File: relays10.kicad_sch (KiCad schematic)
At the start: 40 parts, among them K21 Fujitsu_FTR-LYAA005x, K22 Fujitsu_FTR-LYAA005x, K23 Fujitsu_FTR-LYAA005x, K24 Fujitsu_FTR-LYAA005x, K25 Fujitsu_FTR-LYAA005x, K26 Fujitsu_FTR-LYAA005x, K27 Fujitsu_FTR-LYAA005x, K28 Fujitsu_FTR-LYAA005x, K29 Fujitsu_FTR-LYAA005x, K30 Fujitsu_FTR-LYAA005x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

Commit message: moved to 3v3
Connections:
- net Tr1 renamed Sqr1
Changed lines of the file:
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@@
 		)
 	)
-	(global_label "Tr1"
+	(global_label "Sqr1"
 		(shape input)
 		(at 59.69 74.93 270)
@@
 		)
 		(property "Intersheetrefs" "${INTERSHEET_REFS}"
-			(at 59.69 80.8785 90)
-			(effects
-				(font
-					(size 1.27 1.27)
-				)
-				(justify right)
-				(hide yes)
-			)
-		)
-	)
-	(global_label "Tr1"
+			(at 59.69 82.2694 90)
+			(effects
+				(font
+					(size 1.27 1.27)
+				)
+				(justify right)
+				(hide yes)
+			)
+		)
+	)
+	(global_label "Sqr1"
+		(shape input)
+		(at 149.86 74.93 270)
+		(fields_autoplaced yes)
+		(effects
+			(font
+				(size 1.27 1.27)
+			)
+			(justify right)
+		)
+		(property "Intersheetrefs" "${INTERSHEET_REFS}"
+			(at 149.86 82.2694 90)
+			(effects
+				(font
+					(size 1.27 1.27)
+				)
+				(justify right)
+				(hide yes)
+			)
+		)
+	)
+	(global_label "Sqr1"
 		(shape input)
 		(at 238.76 74.93 270)
@@
 		)
 		(property "Intersheetrefs" "${INTERSHEET_REFS}"
-			(at 238.76 80.8785 90)
-			(effects
-				(font
-					(size 1.27 1.27)
-				)
-				(justify right)
-				(hide yes)
-			)
-		)
-	)
-	(global_label "Tr1"
+			(at 238.76 82.2694 90)
+			(effects
+				(font
+					(size 1.27 1.27)
+				)
+				(justify right)
+				(hide yes)
+			)
+		)
+	)
+	(global_label "Sqr1"
+		(shape input)
+		(at 238.76 132.08 270)
+		(fields_autoplaced yes)
+		(effects
+			(font
+				(size 1.27 1.27)
+			)
+			(justify right)
+		)
+		(property "Intersheetrefs" "${INTERSHEET_REFS}"
+			(at 238.76 139.4194 90)
+			(effects
+				(font
+					(size 1.27 1.27)
+				)
+				(justify right)
+				(hide yes)
+			)
+		)
+	)
+	(global_label "Sqr1"
+		(shape input)
+		(at 194.31 74.93 270)
+		(fields_autoplaced yes)
+		(effects
+			(font
+				(size 1.27 1.27)
+			)
+			(justify right)
+		)
+		(property "Intersheetrefs" "${INTERSHEET_REFS}"
+			(at 194.31 82.2694 90)
+			(effects
+				(font
+					(size 1.27 1.27)
+				)
+				(justify right)
+				(hide yes)
+			)
+		)
+	)
+	(global_label "Sqr1"
+		(shape input)
+		(at 59.69 132.08 270)
+		(fields_autoplaced yes)
+		(effects
+			(font
+				(size 1.27 1.27)
+			)
+			(justify right)
+		)
+		(property "Intersheetrefs" "${INTERSHEET_REFS}"
+			(at 59.69 139.4194 90)
+			(effects
+				(font
+					(size 1.27 1.27)
+				)
+				(justify right)
+				(hide yes)
+			)
+		)
+	)
+	(global_label "Sqr1"
 		(shape input)
 		(at 105.41 132.08 270)
@@
 		)
 		(property "Intersheetrefs" "${INTERSHEET_REFS}"
-			(at 105.41 138.0285 90)
-			(effects
-				(font
-					(size 1.27 1.27)
-				)
-				(justify right)
-				(hide yes)
-			)
-		)
-	)
-	(global_label "Tr1"
+			(at 105.41 139.4194 90)
+			(effects
+				(font
+					(size 1.27 1.27)
+				)
+				(justify right)
+				(hide yes)
+			)
+		)
+	)
+	(global_label "Sqr1"
+		(shape input)
+		(at 194.31 132.08 270)
+		(fields_autoplaced yes)
+		(effects
+			(font
+				(size 1.27 1.27)
+			)
+			(justify right)
+		)
+		(property "Intersheetrefs" "${INTERSHEET_REFS}"
+			(at 194.31 139.4194 90)
+			(effects
+				(font
+					(size 1.27 1.27)
+				)
+				(justify right)
+				(hide yes)
+			)
+		)
+	)
+	(global_label "Sqr1"
+		(shape input)
+		(at 149.86 132.08 270)
+		(fields_autoplaced yes)
+		(effects
+			(font
+				(size 1.27 1.27)
+			)
+			(justify right)
+		)
+		(property "Intersheetrefs" "${INTERSHEET_REFS}"
+			(at 149.86 139.4194 90)
+			(effects
+				(font
+					(size 1.27 1.27)
+				)
+				(justify right)
+				(hide yes)
+			)
+		)
+	)
+	(global_label "Sqr1"
 		(shape input)
 		(at 105.41 74.93 270)
@@
 		)
 		(property "Intersheetrefs" "${INTERSHEET_REFS}"
-			(at 105.41 80.8785 90)
-			(effects
-				(font
-					(size 1.27 1.27)
-				)
-				(justify right)
-				(hide yes)
-			)
-		)
-	)
-	(global_label "Tr1"
-		(shape input)
-		(at 149.86 132.08 270)
-		(fields_autoplaced yes)
-		(effects
-			(font
-				(size 1.27 1.27)
-			)
-			(justify right)
-		)
-		(property "Intersheetrefs" "${INTERSHEET_REFS}"
-			(at 149.86 138.0285 90)
-			(effects
-				(font
-					(size 1.27 1.27)
-				)
-				(justify right)
-				(hide yes)
-			)
-		)
-	)
-	(global_label "Tr1"
-		(shape input)
-		(at 194.31 74.93 270)
-		(fields_autoplaced yes)
-		(effects
-			(font
-				(size 1.27 1.27)
-			)
-			(justify right)
-		)
-		(property "Intersheetrefs" "${INTERSHEET_REFS}"
-			(at 194.31 80.8785 90)
-			(effects
-				(font
-					(size 1.27 1.27)
-				)
-				(justify right)
-				(hide yes)
-			)
-		)
-	)
-	(global_label "Tr1"
-		(shape input)
-		(at 149.86 74.93 270)
-		(fields_autoplaced yes)
-		(effects
-			(font
-				(size 1.27 1.27)
-			)
-			(justify right)
-		)
-		(property "Intersheetrefs" "${INTERSHEET_REFS}"
-			(at 149.86 80.8785 90)
-			(effects
-				(font
-					(size 1.27 1.27)
-				)
-				(justify right)
-				(hide yes)
-			)
-		)
-	)
-	(global_label "Tr1"
-		(shape input)
-		(at 194.31 132.08 270)
-		(fields_autoplaced yes)
-		(effects
-			(font
-				(size 1.27 1.27)
-			)
-			(justify right)
-		)
-		(property "Intersheetrefs" "${INTERSHEET_REFS}"
-			(at 194.31 138.0285 90)
-			(effects
-				(font
-					(size 1.27 1.27)
-				)
-				(justify right)
-				(hide yes)
-			)
-		)
-	)
-	(global_label "Tr1"
-		(shape input)
-		(at 238.76 132.08 270)
-		(fields_autoplaced yes)
-		(effects
-			(font
-				(size 1.27 1.27)
-			)
-			(justify right)
-		)
-		(property "Intersheetrefs" "${INTERSHEET_REFS}"
-			(at 238.76 138.0285 90)
-			(effects
-				(font
-					(size 1.27 1.27)
-				)
-				(justify right)
-				(hide yes)
-			)
-		)
-	)
-	(global_label "Tr1"
-		(shape input)
-		(at 59.69 132.08 270)
-		(fields_autoplaced yes)
-		(effects
-			(font
-				(size 1.27 1.27)
-			)
-			(justify right)
-		)
-		(property "Intersheetrefs" "${INTERSHEET_REFS}"
-			(at 59.69 138.0285 90)
-			(effects
-				(font
+			(at 105.41 82.2694 90)
+			(effects
+				(font

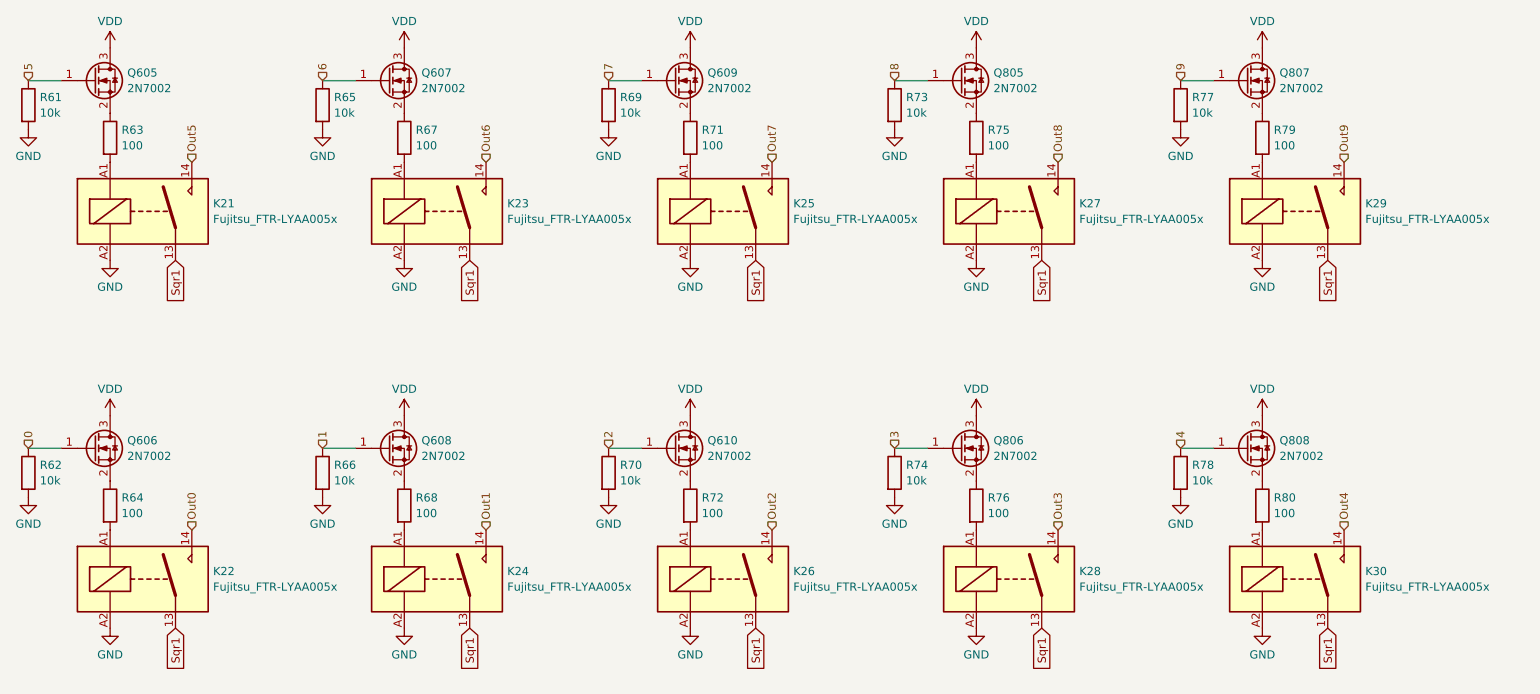
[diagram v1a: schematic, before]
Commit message: added decoupling caps
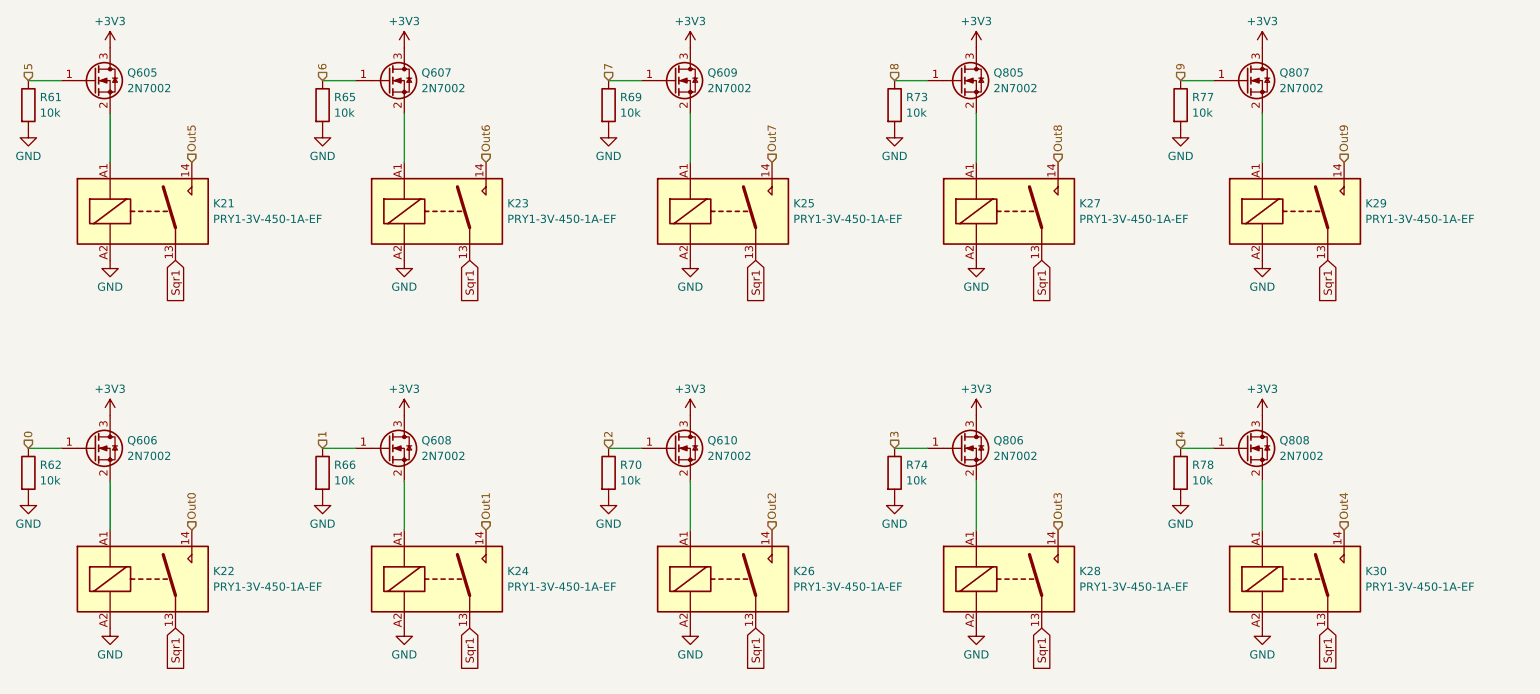
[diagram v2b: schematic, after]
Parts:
- removed R63, R64, R67, R68, R71, R72, R75, R76, R79, R80: 100, Resistor_SMD:R_0402_1005Metric, symbol Device:R
- K21, K22, K23, K24, K25, K26, K27, K28, K29, K30: value Fujitsu_FTR-LYAA005x -> PRY1-3V-450-1A-EF
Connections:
- net at Q605.2 (S): now also K21.A1
- net at Q606.2 (S): now also K22.A1
- net at K24.A1: now also Q608.2 (S)
- net at Q805.2 (S): now also K27.A1
- net at K30.A1: now also Q808.2 (S)
- net at K28.A1: now also Q806.2 (S)
- net at Q607.2 (S): now also K23.A1
- net at K25.A1: now also Q609.2 (S)
- net at Q807.2 (S): now also K29.A1
- net at K26.A1: now also Q610.2 (S)
- net VDD renamed +3V3

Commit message: corrected output/input type of pins
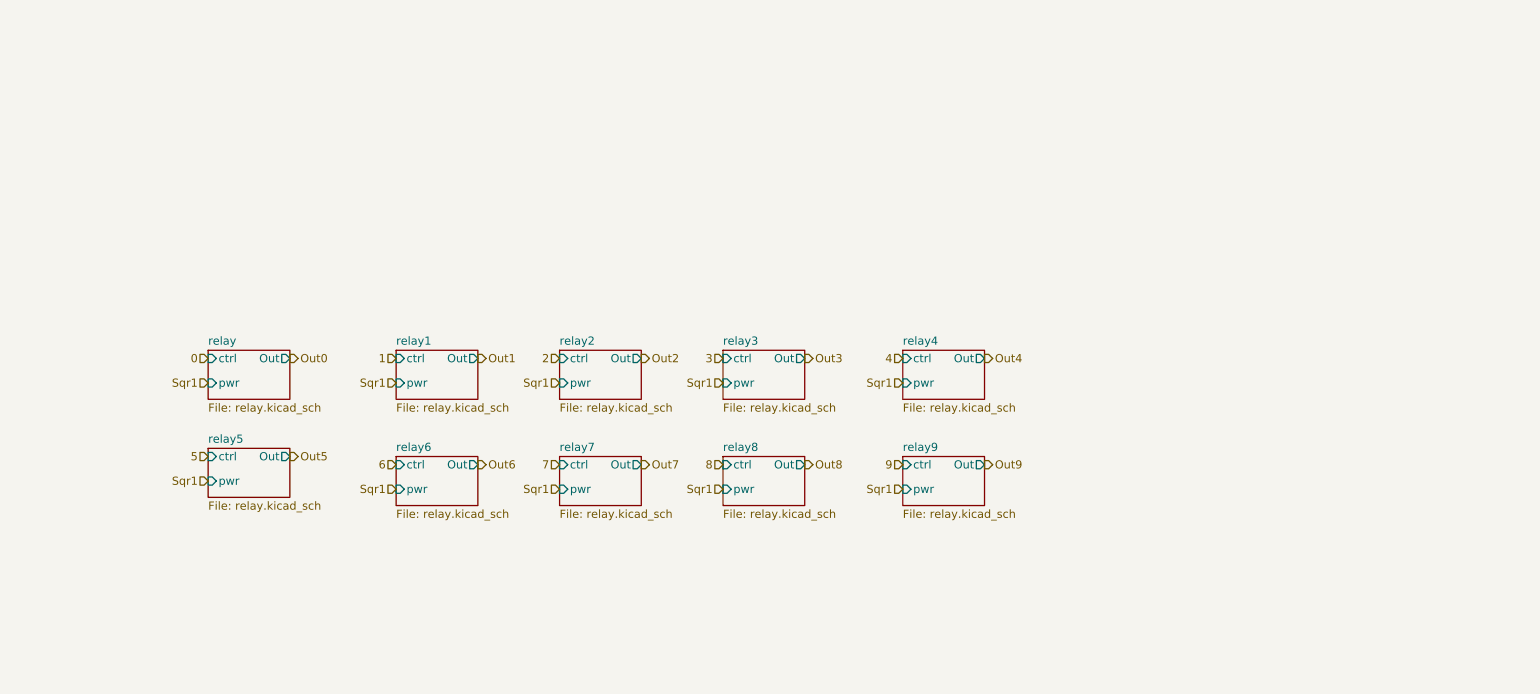
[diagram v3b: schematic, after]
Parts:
- removed K21, K22, K23, K24, K25, K26, K27, K28, K29, K30: PRY1-3V-450-1A-EF, Relay_THT:Relay_SPST-NO_Fujitsu_FTR-LYAA005x_FormA_Vertical, symbol Relay:Fujitsu_FTR-LYAA005x
- removed Q605, Q606, Q607, Q608, Q609, Q610, Q805, Q806, Q807, Q808: 2N7002, Package_TO_SOT_SMD:SOT-23, symbol Transistor_FET:2N7002
- removed R61, R62, R65, R66, R69, R70, R73, R74, R77, R78: 10k, Resistor_SMD:R_0402_1005Metric, symbol Device:R
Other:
- added sheet relay (relay.kicad_sch)
- added sheet relay1 (relay.kicad_sch)
- added sheet relay2 (relay.kicad_sch)
- added sheet relay3 (relay.kicad_sch)
- added sheet relay4 (relay.kicad_sch)
- added sheet relay5 (relay.kicad_sch)
- added sheet relay6 (relay.kicad_sch)
- added sheet relay7 (relay.kicad_sch)
- added sheet relay8 (relay.kicad_sch)
- added sheet relay9 (relay.kicad_sch)

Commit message: schematic cleanup, routed 1 bdc
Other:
- removed sheet relay
- removed sheet relay1
- removed sheet relay2
- removed sheet relay3
- removed sheet relay4
- removed sheet relay5
- removed sheet relay6
- removed sheet relay7
- removed sheet relay8
- removed sheet relay9
- added sheet SSR (ssr.kicad_sch)
- added sheet SSR1 (ssr.kicad_sch)
- added sheet SSR2 (ssr.kicad_sch)
- added sheet SSR3 (ssr.kicad_sch)
- added sheet SSR4 (ssr.kicad_sch)
- added sheet SSR5 (ssr.kicad_sch)
- added sheet SSR6 (ssr.kicad_sch)
- added sheet SSR7 (ssr.kicad_sch)
- added sheet SSR8 (ssr.kicad_sch)
- added sheet SSR9 (ssr.kicad_sch)

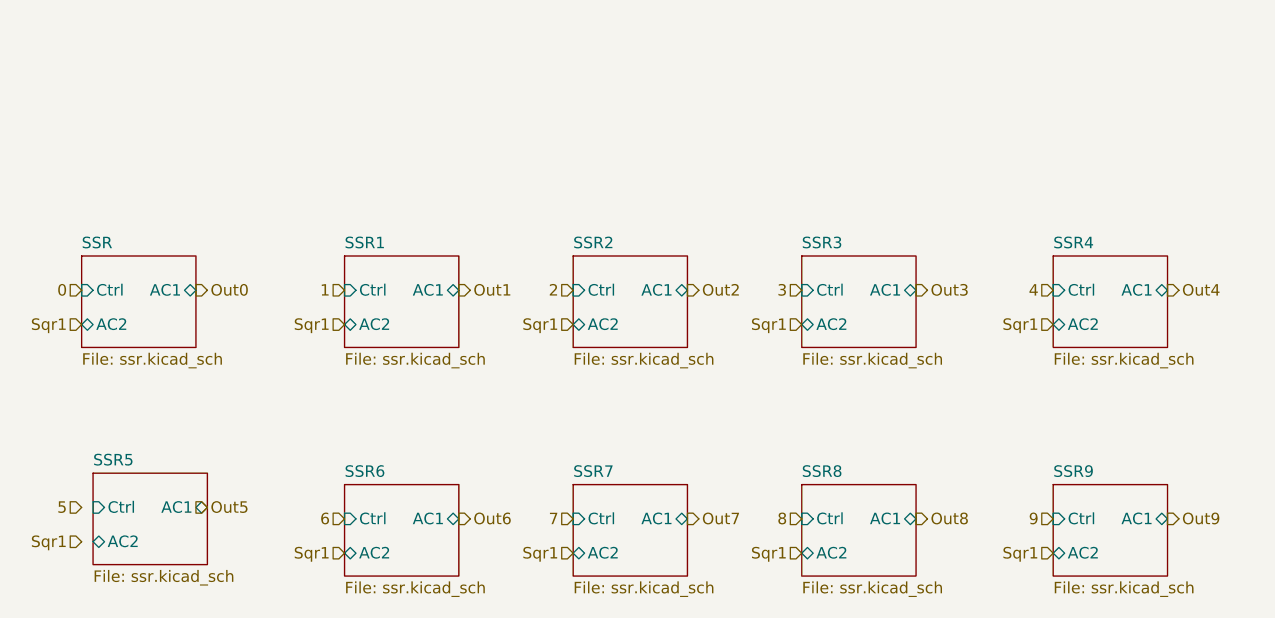
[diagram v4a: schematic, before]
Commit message: switched to using SSR module
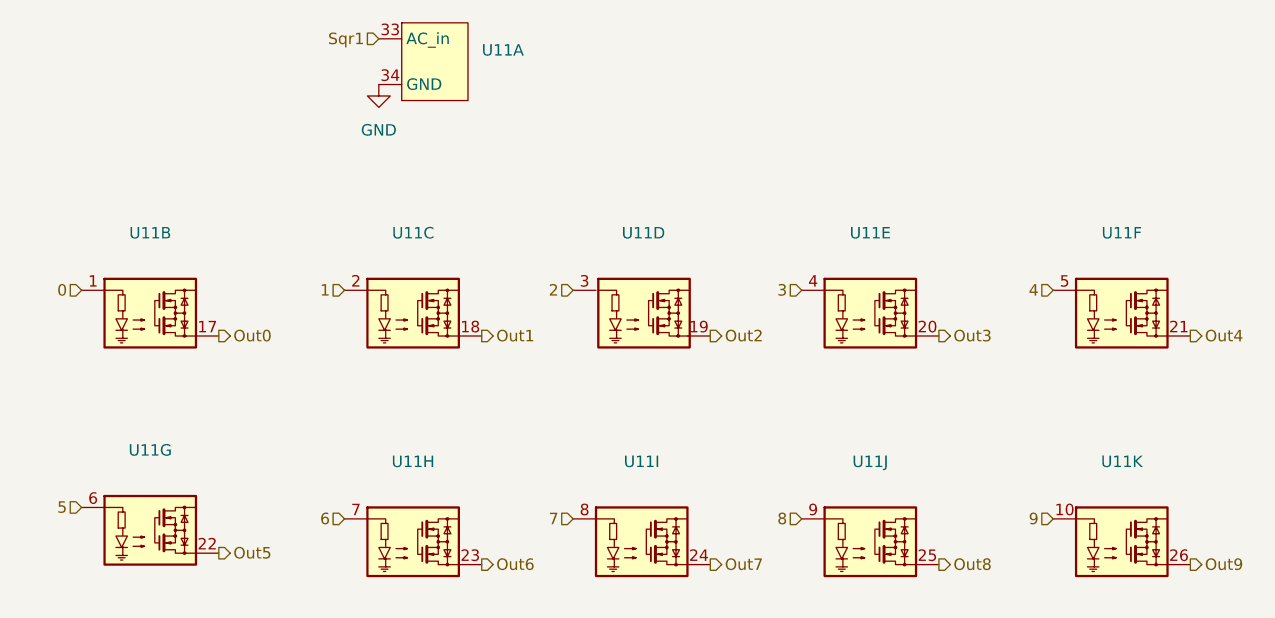
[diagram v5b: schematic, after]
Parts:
- added U11: ~, symbol custom:SSR
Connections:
- net 0: now also U11.1
- net 1: now also U11.2
- net 2: now also U11.3
- net 3: now also U11.4
- net 4: now also U11.5
- net 5: now also U11.6
- net 6: now also U11.7
- net 7: now also U11.8
- net 8: now also U11.9
- net 9: now also U11.10
- net Out0: now also U11.17
- net Out1: now also U11.18
- net Out2: now also U11.19
- net Out3: now also U11.20
- net Out4: now also U11.21
- net Out5: now also U11.22
- net Out6: now also U11.23
- net Out7: now also U11.24
- net Out8: now also U11.25
- net Out9: now also U11.26
- net Sqr1: now also U11.33 (AC_in)
- new net GND: U11.34 (GND)
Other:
- removed sheet SSR
- removed sheet SSR1
- removed sheet SSR2
- removed sheet SSR3
- removed sheet SSR4
- removed sheet SSR5
- removed sheet SSR6
- removed sheet SSR7
- removed sheet SSR8
- removed sheet SSR9

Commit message: added footprints for modules
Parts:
- U2: renamed from U11; footprint (none) -> custom:module_ssr
